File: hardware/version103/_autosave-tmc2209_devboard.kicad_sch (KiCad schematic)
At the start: 22 parts, among them J1 Conn_02x05_Odd_Even, J2 Screw_Terminal_01x04, J3 Conn_01x02_Socket, U1 TMC2209-LA

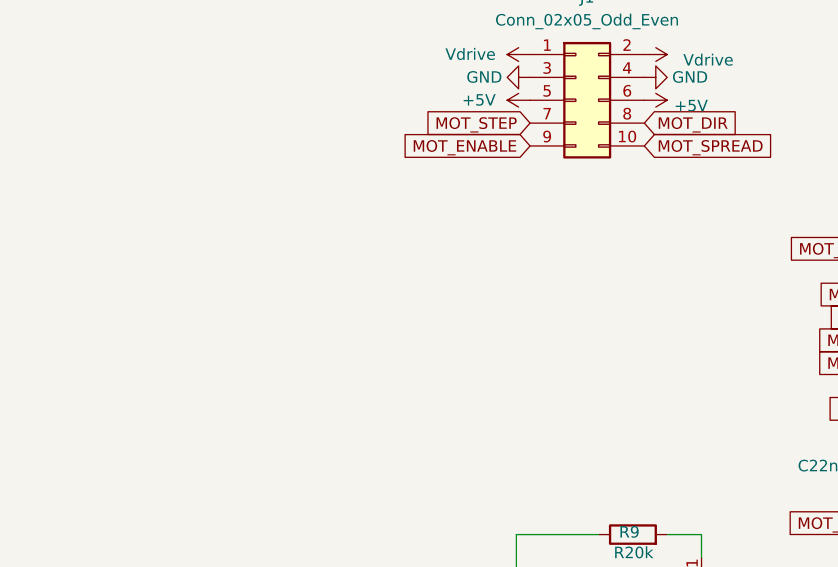
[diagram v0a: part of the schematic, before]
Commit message: Add files via upload
An edited version of Version103 which measures 45x45mm  This one has been ordered through JLCPCB and successfully tested.
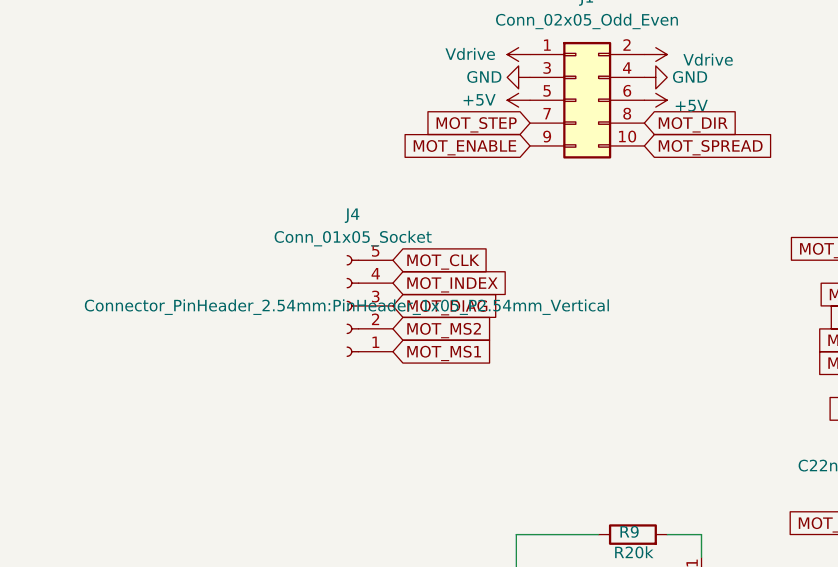
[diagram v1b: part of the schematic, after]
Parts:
- added J4: Conn_01x05_Socket, Connector_PinHeader_2.54mm:PinHeader_1x05_P2.54mm_Vertical, symbol Connector:Conn_01x05_Socket
- J1: LCSC (none) -> C2685327
- J2: LCSC (none) -> C3034542
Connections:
- net MOT_CLK: now also J4.5 (Pin_5)
- net MOT_DIAG: now also J4.3 (Pin_3)
- net MOT_INDEX: now also J4.4 (Pin_4)
- net MOT_MS1: now also J4.1 (Pin_1)
- net MOT_MS2: now also J4.2 (Pin_2)
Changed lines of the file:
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@@
+    )
+  )
+  (global_label "MOT_MS2" (shape input) (at 33.02 60.96 0) (fields_autoplaced)
+    (effects (font (size 1.27 1.27)) (justify left))
+    (property "Intersheetrefs" "${INTERSHEET_REFS}" (at 43.8591 60.96 0)
+      (effects (font (size 1.27 1.27)) (justify left) hide)
     )
   )
@@
     )
   )
+  (global_label "MOT_MS1" (shape input) (at 33.02 63.5 0) (fields_autoplaced)
+    (effects (font (size 1.27 1.27)) (justify left))
+    (property "Intersheetrefs" "${INTERSHEET_REFS}" (at 43.8591 63.5 0)
+      (effects (font (size 1.27 1.27)) (justify left) hide)
+    )
+  )
   (global_label "OA2" (shape input) (at 141.478 69.85 0) (fields_autoplaced)
     (effects (font (size 1.27 1.27)) (justify left))
@@
     )
   )
+  (global_label "MOT_INDEX" (shape input) (at 33.02 55.88 0) (fields_autoplaced)
+    (effects (font (size 1.27 1.27)) (justify left))
+    (property "Intersheetrefs" "${INTERSHEET_REFS}" (at 45.5525 55.88 0)
+      (effects (font (size 1.27 1.27)) (justify left) hide)
+    )
+  )
   (global_label "MOT_DIR" (shape input) (at 60.96 38.1 0) (fields_autoplaced)
     (effects (font (size 1.27 1.27)) (justify left))
@@
     )
   )
+  (global_label "MOT_CLK" (shape input) (at 33.02 53.34 0) (fields_autoplaced)
+    (effects (font (size 1.27 1.27)) (justify left))
+    (property "Intersheetrefs" "${INTERSHEET_REFS}" (at 43.5568 53.34 0)
+      (effects (font (size 1.27 1.27)) (justify left) hide)
+    )
+  )
   (global_label "MOT_STEP" (shape input) (at 48.26 38.1 180) (fields_autoplaced)
     (effects (font (size 1.27 1.27)) (justify right))
@@
     )
   )
+  (global_label "MOT_DIAG" (shape input) (at 33.02 58.42 0) (fields_autoplaced)
+    (effects (font (size 1.27 1.27)) (justify left))
+    (property "Intersheetrefs" "${INTERSHEET_REFS}" (at 44.2221 58.42 0)
+      (effects (font (size 1.27 1.27)) (justify left) hide)
+    )
+  )
   (global_label "OA1" (shape input) (at 141.478 64.77 0) (fields_autoplaced)
     (effects (font (size 1.27 1.27)) (justify left))
@@
     )
     (property "Datasheet" "~" (at 53.34 35.56 0)
+      (effects (font (size 1.27 1.27)) hide)
+    )
+    (property "LCSC" "C2685327" (at 53.34 35.56 0)
       (effects (font (size 1.27 1.27)) hide)
     )
@@
         (path "/269f19c3-6824-45a8-be29-fa58d70cbb42"
           (reference "#PWR07") (unit 1)
+        )
+      )
+    )
+  )
+  (symbol (lib_id "Connector:Conn_01x05_Socket") (at 27.94 58.42 180) (unit 1)
+    (in_bom yes) (on_board yes) (dnp no) (fields_autoplaced)
+    (property "Reference" "J4" (at 28.575 48.26 0)
+      (effects (font (size 1.27 1.27)))
+    )
+    (property "Value" "Conn_01x05_Socket" (at 28.575 50.8 0)
+      (effects (font (size 1.27 1.27)))
+    )
+    (property "Footprint" "Connector_PinHeader_2.54mm:PinHeader_1x05_P2.54mm_Vertical" (at 27.94 58.42 0)
+      (effects (font (size 1.27 1.27)))
+    )
+    (property "Datasheet" "~" (at 27.94 58.42 0)
+      (effects (font (size 1.27 1.27)) hide)
+    )
+    (pin "1")
+    (pin "2")
+    (pin "3")
+    (pin "4")
+    (pin "5")
+    (instances
+      (project "tmc2209_devboard"
+        (path "/269f19c3-6824-45a8-be29-fa58d70cbb42"
+          (reference "J4") (unit 1)
         )
       )
@@
       (effects (font (size 1.27 1.27)) hide)
     )
+    (property "LCSC" "C3034542" (at 207.01 93.98 0)
+      (effects (font (size 1.27 1.27)) hide)
+    )
